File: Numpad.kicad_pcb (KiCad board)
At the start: 2 copper layers, 83.2 x 98.2 mm, 106 parts, among them J1 USB_C_Receptacle_USB2.0, J3 AVR-ISP-6, Q2 DMN2041L, SW10 SW_Push, SW11 SW_Push, SW12 SW_Push, SW13 SW_Push, SW14 SW_Push, SW15 SW_Push, SW16 SW_Push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

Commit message: redid the numpad quite a bit, including improving the usb and layout
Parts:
- H5: renamed from Kailh PG1350; value Choc -> Kailh PG1350 Stabilizer 2U Vert; footprint Keebio-Parts:Kailh-PG1350-2u-Custom -> Keebio-Parts:Kailh-Stabilizer-2u-Vert
- J1: footprint Connector_USB:USB_C_Receptacle_HRO_TYPE-C-31-M-12 -> Type-C:HRO-TYPE-C-31-M-13
- SW_RESET1: footprint Button_Switch_SMD:SW_SPST_SKQG_WithStem -> Keebio-Parts:SW_SPST_TL3342
- moved D125 111.7 mm to (150.2, 18.6)
- moved Q2 102.3 mm to (149.7, 11.8)
- moved R3 102.3 mm to (155.7, 16.6)
- moved C4 82.6 mm to (133.1, -4.43)
- moved C1 80.9 mm to (135.4, -10.2)
- moved C6 80.9 mm to (143.2, 18.7)
- moved C7 80.9 mm to (149.5, -1.01)
- moved R6 80.9 mm to (145.7, -9.77)
- moved C3 78.5 mm to (131.1, 15.3)
- moved C5 78.5 mm to (127.1, 19.3)
- moved Y1 78.5 mm to (129.1, 17.3)
- moved C2 78.5 mm to (127.3, 15.4)
- moved R23 74.0 mm to (135.6, 0.89)
- moved R34 72.8 mm to (140.4, 14.3)
- moved R1 72.2 mm to (130.8, 5.40)
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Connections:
- D1 pad 2: D- -> D+
- D1 pad 3: D+ -> D-
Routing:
- net RGB: track 121.9 -> 0.00 mm, vias 2 -> 0
- net RST: track 77.6 -> 0.00 mm, vias 1 -> 0
- net ROW_4: track 110.1 -> 54.0 mm, vias 2 -> 0
- net MISO: track 48.6 -> 0.00 mm, vias 1 -> 0
- net SCLK: track 41.8 -> 0.00 mm, vias 1 -> 0
- net ROW_3: track 95.4 -> 54.0 mm, vias 2 -> 0
- net MOSI: track 40.1 -> 0.00 mm, vias 1 -> 0
- net ROW_2: track 89.1 -> 54.0 mm
- net ROW_0: track 68.5 -> 47.0 mm
- net VCC: track 0.00 -> 21.3 mm, vias 0 -> 3
- net ROW_1: track 57.8 -> 36.5 mm
- net D33: track 87.6 -> 73.6 mm
- net D25: track 87.6 -> 73.7 mm
- net D29: track 87.5 -> 73.6 mm
- net D37: track 69.4 -> 55.6 mm
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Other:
- board size 83.2 x 98.2 mm -> 75 x 104 mm

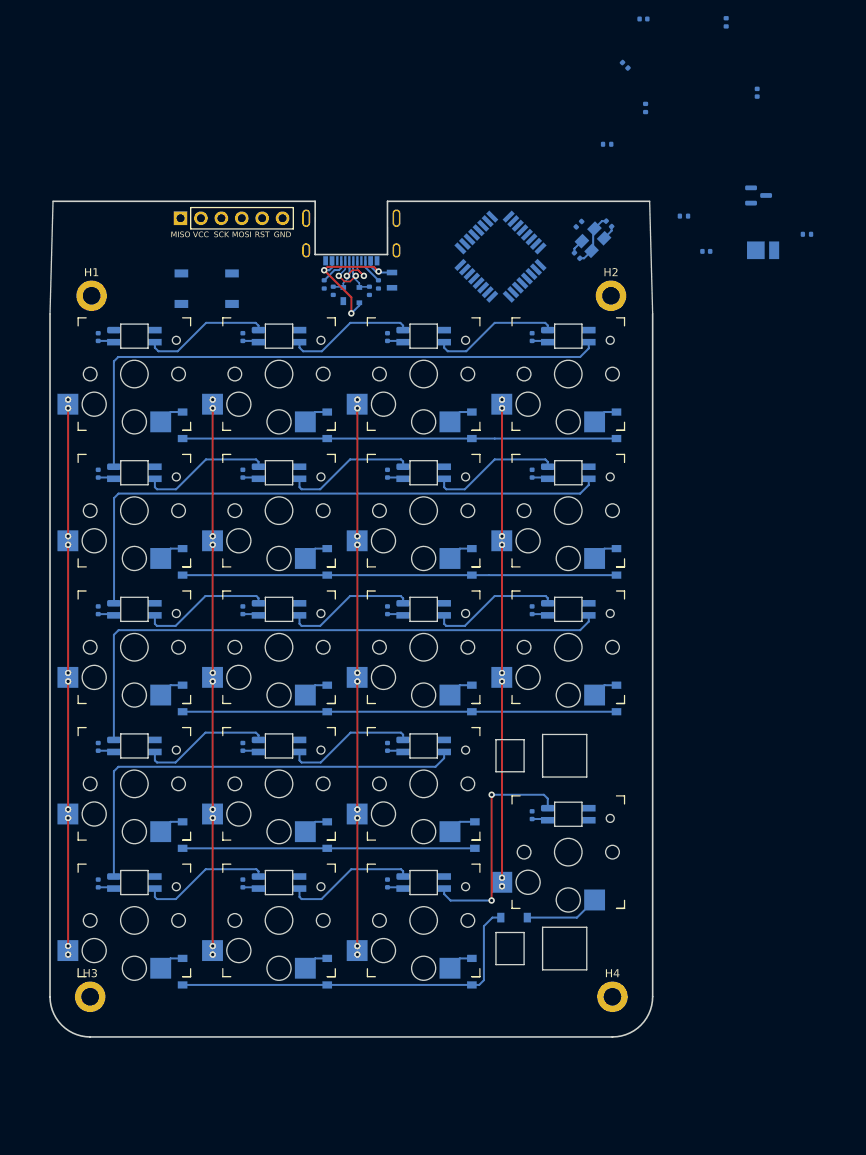
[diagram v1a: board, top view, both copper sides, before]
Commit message: did a lot of work on the numpad, basically it's "finished"
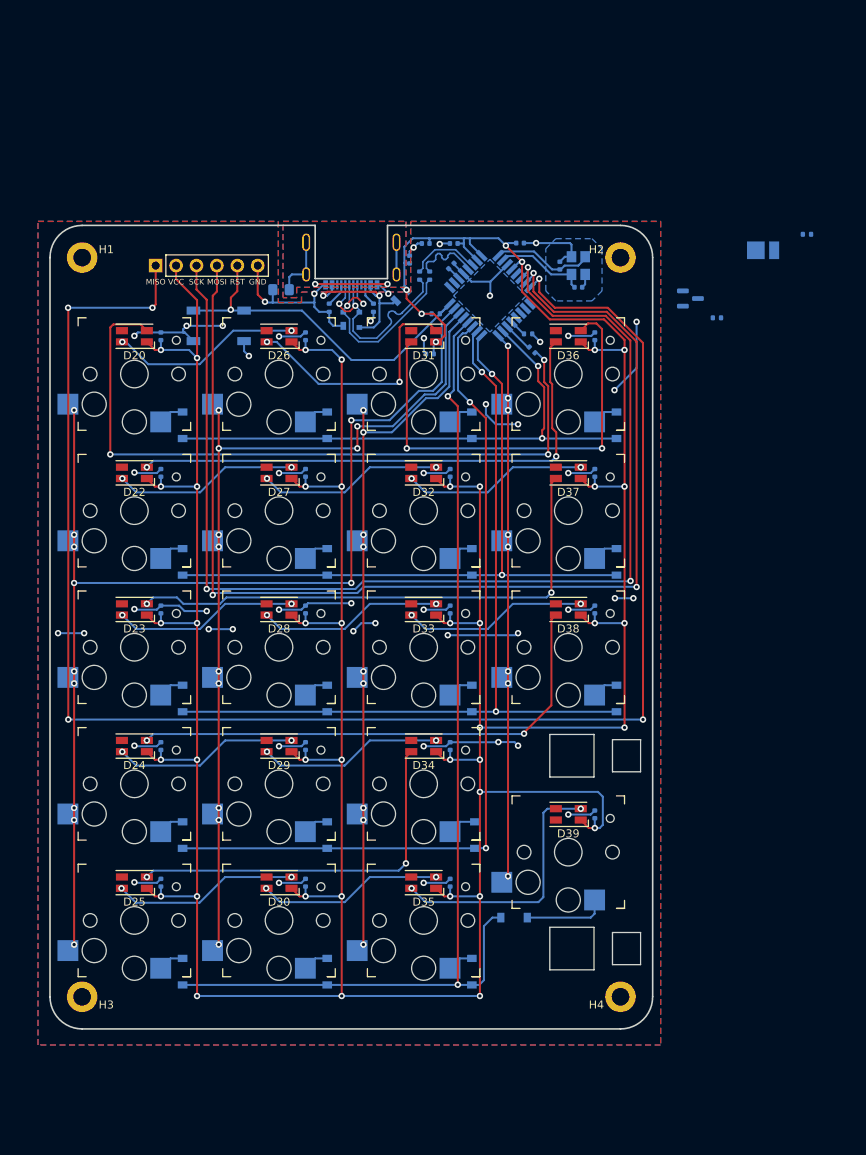
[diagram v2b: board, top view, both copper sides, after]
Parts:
- added FB1: FerriteBead_Small, Inductor_SMD:L_0805_2012Metric_Pad1.15x1.40mm_HandSolder, B.Cu at (90.2, 23.5)
- D20, D22, D23, D24, D25, D26, D27, D28, D29, D30, D31, D32, D33, D34, D35, D36, D37, D38, D39: value SK6812MINI -> NeoPixel_THT; footprint Keebio-Parts:SK6812-MINI-E -> kicad-keyboard-parts.pretty:LED_RGB_Wuerth-PLCC4_3.2x2.8mm_150141M173100; moved to F.Cu
- moved D24 74.3 mm to (72.0, 80.3)
- moved D37 74.3 mm to (126.0, 46.3)
- moved D36 59.5 mm to (126.0, 29.3)
- moved D25 51.0 mm to (72.0, 97.3)
- moved D23 49.5 mm to (72.0, 63.3)
- moved D38 49.5 mm to (126.0, 63.3)
- moved C7 45.3 mm to (108.2, 17.8), turned to 180 degrees
- moved C1 41.8 mm to (106.2, 19.8), turned to 90 degrees
- moved D28 39.8 mm to (90.0, 63.3)
- moved D33 39.8 mm to (108.0, 63.3)
- moved R6 36.8 mm to (144.5, 27.0), turned to 180 degrees
- moved R23 36.6 mm to (109.5, 26.5), turned to 0 degrees
- moved D30 34.0 mm to (90.0, 97.3)
- moved D31 34.0 mm to (108.0, 29.3)
- moved C4 33.0 mm to (111.5, 20.6), turned to 45 degrees
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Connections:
- net Net-(R2-Pad2) renamed D_P
- net Net-(R44-Pad2) renamed D_N
- D20 pad 3: RGB -> +5V
- D20 pad 4: +5V -> RGB
- D22 pad 3: Net-(D20-Pad1) -> +5V
- D22 pad 4: +5V -> D25
- D23 pad 3: Net-(D22-Pad1) -> +5V
- D23 pad 4: +5V -> D29
- D24 pad 1: D25 -> Net-(D24-Pad1)
- D24 pad 3: Net-(D23-Pad1) -> +5V
- D24 pad 4: +5V -> D33
- D25 pad 3: D25 -> +5V
- D25 pad 4: +5V -> D37
- D26 pad 3: Net-(D25-Pad1) -> +5V
- D26 pad 4: +5V -> Net-(D20-Pad1)
- D27 pad 3: Net-(D26-Pad1) -> +5V
- D27 pad 4: +5V -> Net-(D22-Pad1)
- D28 pad 1: D29 -> Net-(D28-Pad1)
- D28 pad 3: Net-(D27-Pad1) -> +5V
- D28 pad 4: +5V -> Net-(D23-Pad1)
- D29 pad 3: D29 -> +5V
- D29 pad 4: +5V -> Net-(D24-Pad1)
- D30 pad 3: Net-(D29-Pad1) -> +5V
- D30 pad 4: +5V -> Net-(D25-Pad1)
- D31 pad 3: Net-(D30-Pad1) -> +5V
- D31 pad 4: +5V -> Net-(D26-Pad1)
- D32 pad 1: D33 -> Net-(D32-Pad1)
- D32 pad 3: Net-(D31-Pad1) -> +5V
- D32 pad 4: +5V -> Net-(D27-Pad1)
- D33 pad 3: D33 -> +5V
- D33 pad 4: +5V -> Net-(D28-Pad1)
- D34 pad 1: Net-(D34-Pad1) -> D37
- D34 pad 3: Net-(D33-Pad1) -> +5V
- D34 pad 4: +5V -> Net-(D29-Pad1)
- D35 pad 1: D37 -> Net-(D35-Pad1)
- D35 pad 3: Net-(D34-Pad1) -> +5V
- D35 pad 4: +5V -> Net-(D30-Pad1)
- D36 pad 1: unconnected-(D36-Pad1) -> D25
- D36 pad 3: Net-(D36-Pad3) -> +5V
- D36 pad 4: +5V -> Net-(D31-Pad1)
- D37 pad 1: Net-(D37-Pad1) -> D29
- D37 pad 3: D37 -> +5V
- D37 pad 4: +5V -> Net-(D32-Pad1)
- D38 pad 1: Net-(D38-Pad1) -> D33
- D38 pad 3: Net-(D37-Pad1) -> +5V
- D38 pad 4: +5V -> Net-(D33-Pad1)
- D39 pad 1: Net-(D36-Pad3) -> unconnected-(D39-Pad1)
- D39 pad 3: Net-(D38-Pad1) -> +5V
- D39 pad 4: +5V -> Net-(D35-Pad1)
- J1 pad S1: GND -> Earth
- R34 pad 1: Net-(R34-Pad1) -> GND
- R34 pad 2: GND -> Net-(R34-Pad2)
- U1 pad 11: ROW_1 -> unconnected-(U1-Pad11)
- U1 pad 12: ROW_2 -> NUM_LOCK_PWM
- U1 pad 13: Net-(R34-Pad1) -> Net-(R34-Pad2)
- U1 pad 14: ROW_3 -> Net-(R1-Pad1)
- U1 pad 16: unconnected-(U1-Pad16) -> COL_3
- U1 pad 17: COL_0 -> ROW_3
- U1 pad 18: COL_1 -> ROW_2
- U1 pad 19: COL_2 -> ROW_1
- U1 pad 20: COL_3 -> ROW_0
- U1 pad 21: NUM_LOCK_PWM -> COL_2
- U1 pad 22: unconnected-(U1-Pad22) -> COL_1
- U1 pad 23: Net-(R1-Pad1) -> COL_0
- U1 pad 9: ROW_0 -> unconnected-(U1-Pad9)
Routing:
- net +5V: track 38.5 -> 553.1 mm, vias 0 -> 46
- net MISO: track 0.00 -> 204.3 mm, vias 0 -> 5
- net GND: track 7.20 -> 185.1 mm, vias 0 -> 49
- net MOSI: track 0.00 -> 144.3 mm, vias 0 -> 3
- net SCLK: track 0.00 -> 143.9 mm, vias 0 -> 3
- net RGB: track 0.00 -> 88.8 mm, vias 0 -> 3
- net ROW_0: track 47.0 -> 131.0 mm, vias 0 -> 2
- net COL_0: track 63.8 -> 144.3 mm, vias 10 -> 11
- net ROW_1: track 36.5 -> 105.1 mm, vias 0 -> 2
- net ROW_2: track 54.0 -> 102.7 mm, vias 0 -> 2
- net COL_1: track 63.8 -> 109.2 mm, vias 10 -> 11
- net RST: track 0.00 -> 44.9 mm, vias 0 -> 1
- net Net-(D31-Pad1): track 16.4 -> 55.9 mm, vias 0 -> 2
- net Net-(D35-Pad1): track 0.00 -> 32.7 mm, vias 0 -> 2
- net ROW_3: track 54.0 -> 84.5 mm, vias 0 -> 2
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- added copper zone on B.Cu, net Earth
- added copper zone on F.Cu, net Earth
- added copper zone on B.Cu, net GND
- added copper zone on F.Cu, net GND
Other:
- board size 75 x 104 mm -> 75 x 100 mm

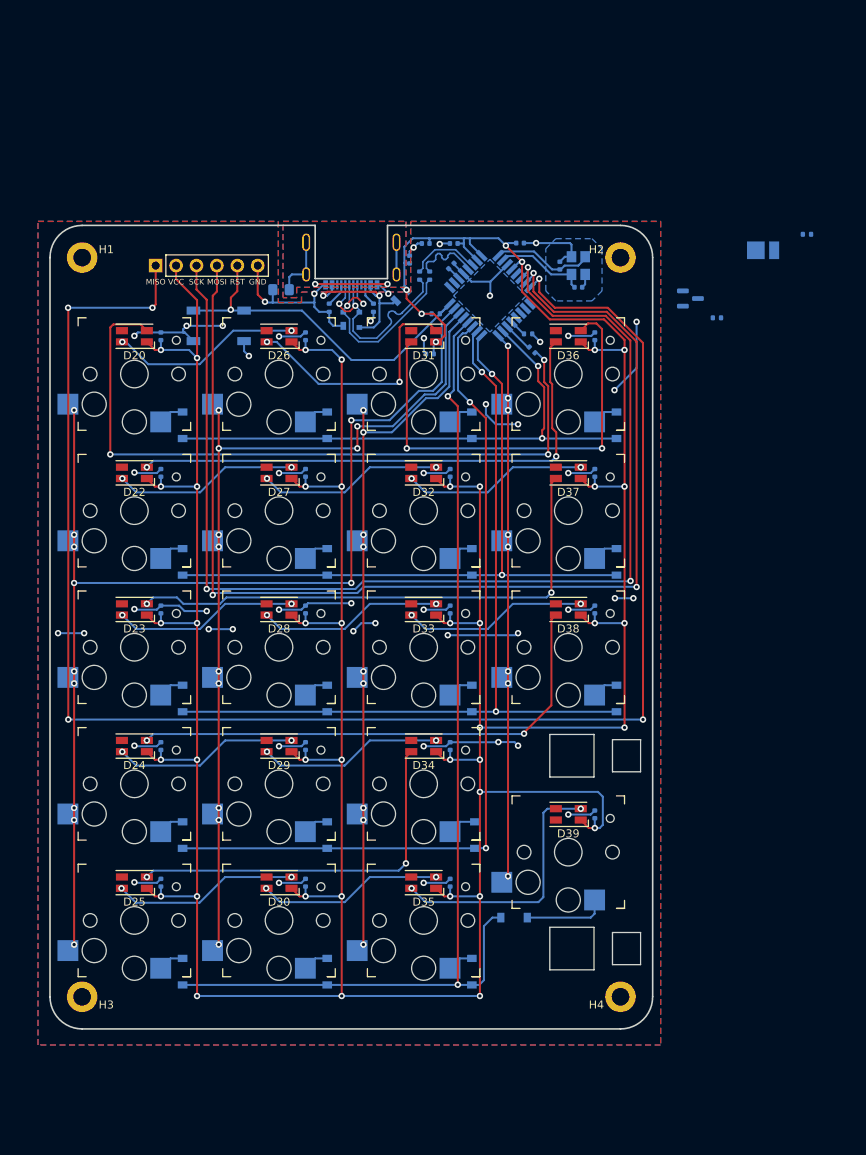
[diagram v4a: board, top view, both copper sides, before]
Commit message: Updated numpad's power traces to be thicker
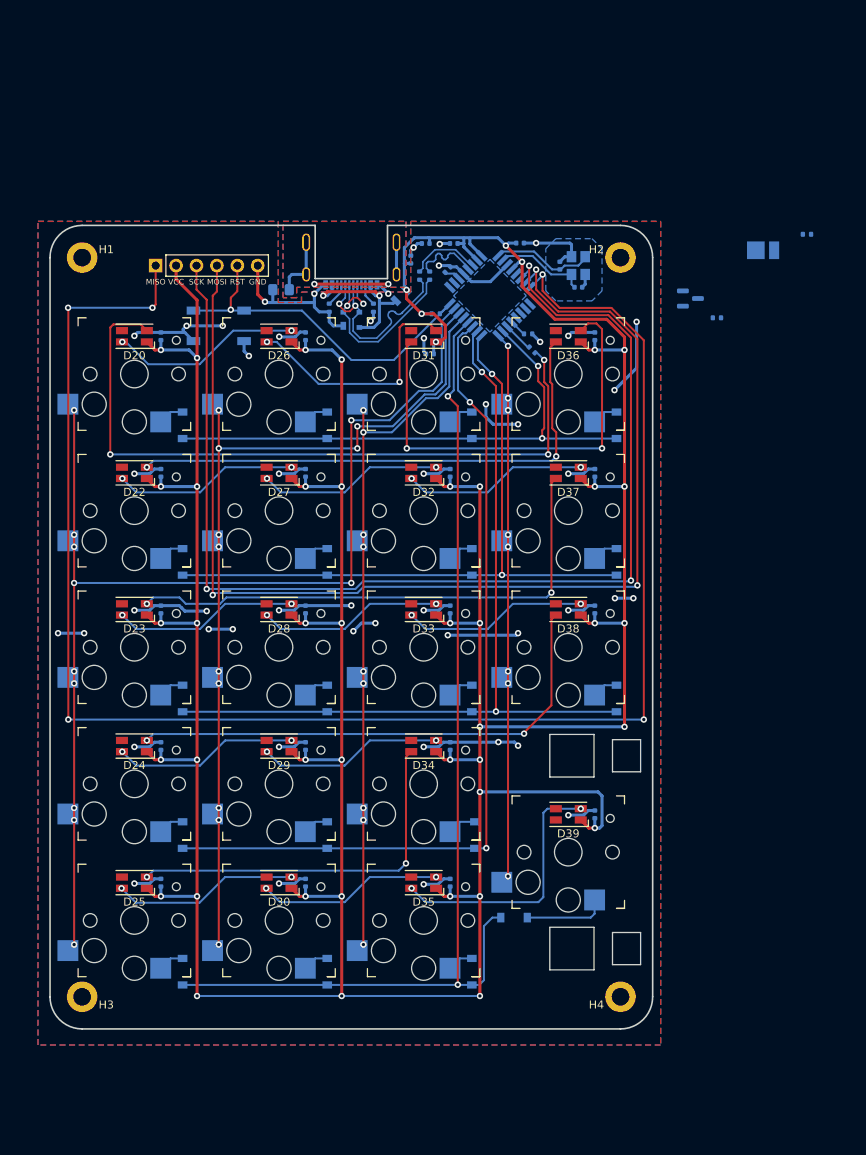
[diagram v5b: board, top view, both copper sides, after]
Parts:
- moved C4 0.64 mm to (111.0, 21.0)
- moved C1 0.15 mm to (106.4, 19.8)
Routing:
- net MISO: track 204.3 -> 205.4 mm
- net MOSI: track 144.3 -> 145.1 mm
- net +5V: track 553.1 -> 553.8 mm
- net GND: track 185.1 -> 185.7 mm

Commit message: made some footprint changes
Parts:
- removed H5: Kailh PG1350 Stabilizer 2U Vert, Keebio-Parts:Kailh-Stabilizer-2u-Vert
- SW21: footprint keyswitches.pretty-2:Kailh_socket_PG1350 -> keyswitches.pretty-2:Kailh_socket_PG1350_2U_Vert

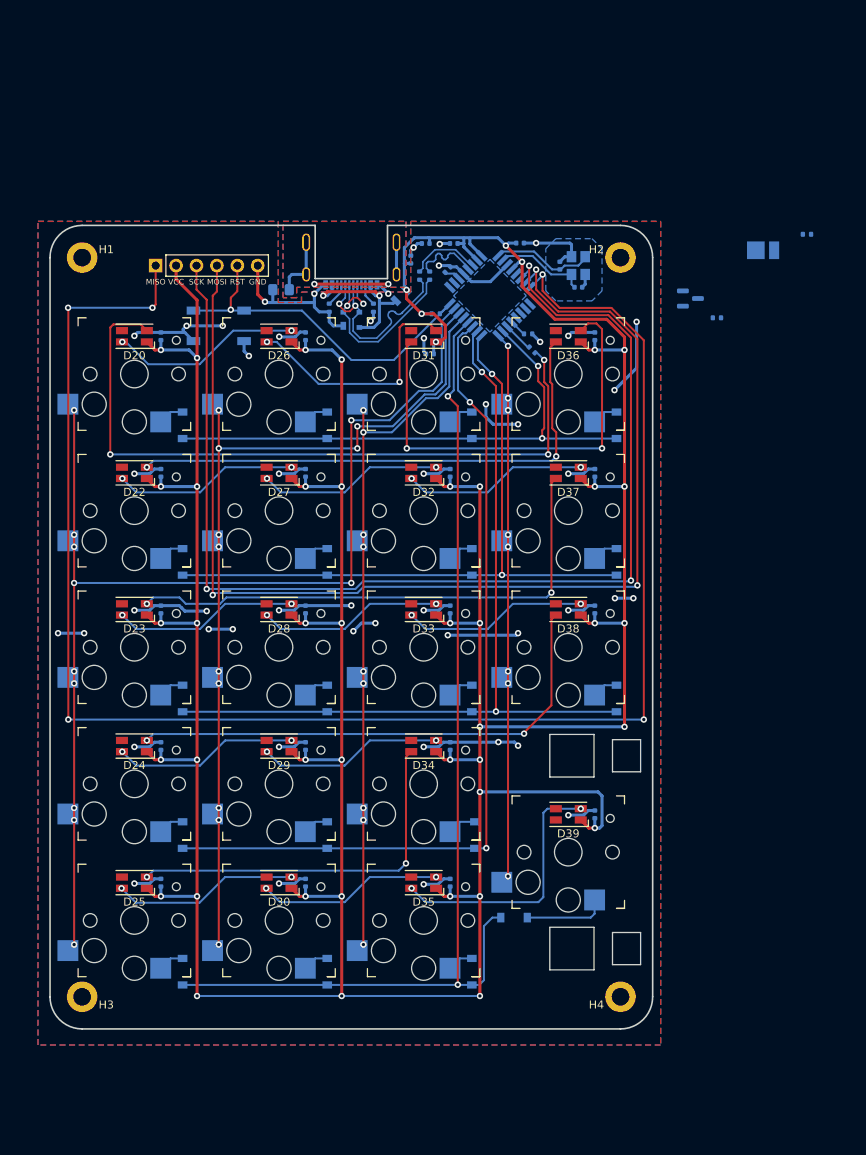
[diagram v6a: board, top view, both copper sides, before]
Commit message: did some via adjustments and decided to not go ahead with num lock light
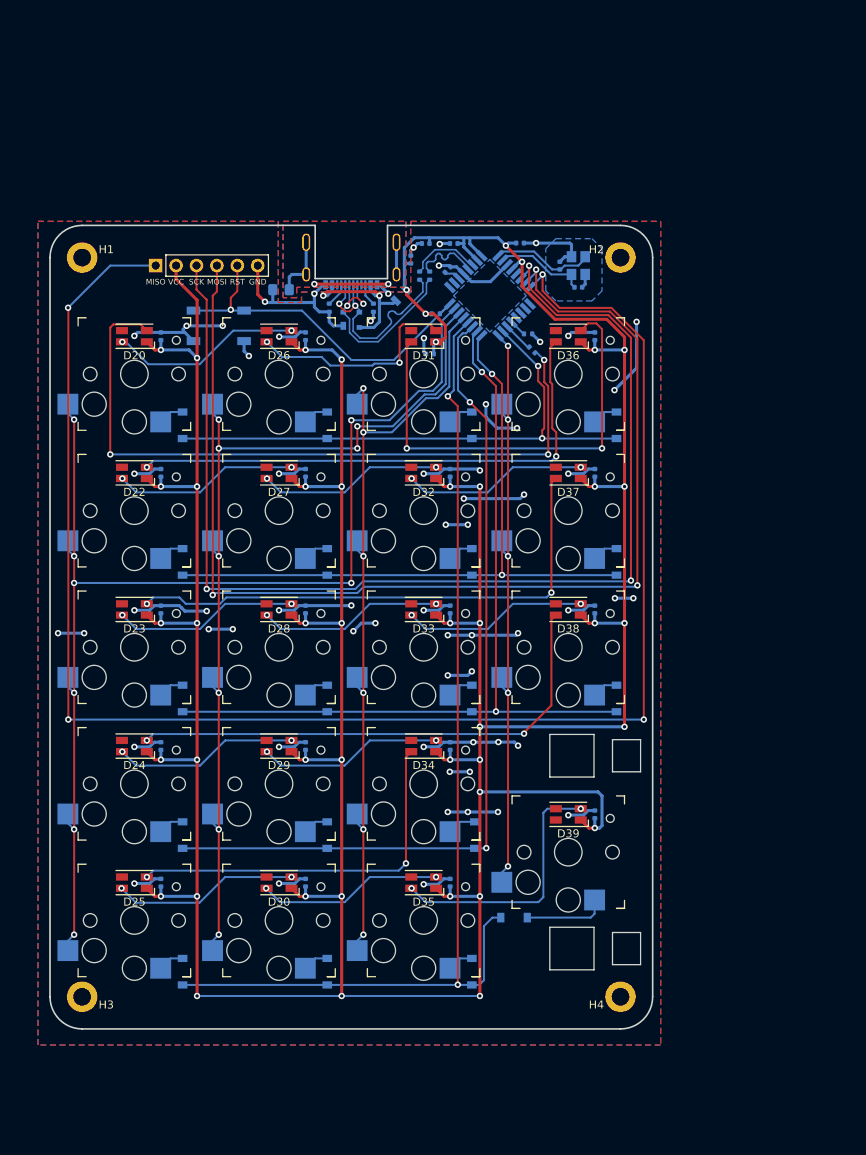
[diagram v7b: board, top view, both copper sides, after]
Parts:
- removed D125: LED, LED_SMD:LED_PLCC_2835
- removed Q2: DMN2041L, Package_TO_SOT_SMD:SOT-23
- removed R3: 470, Resistor_SMD:R_0402_1005Metric
- removed R6: 1k, Resistor_SMD:R_0402_1005Metric
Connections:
- net COL_0 renamed /COL_0
- net COL_1 renamed /COL_1
- net COL_2 renamed /COL_2
- net COL_3 renamed /COL_3
- net D+ renamed /D+
- net D- renamed /D-
- net D25 renamed /D25
- net D29 renamed /D29
- net D33 renamed /D33
- net D37 renamed /D37
- net D_N renamed /D_N
- net D_P renamed /D_P
- net MISO renamed /MISO
- net MOSI renamed /MOSI
- net RGB renamed /RGB
- net ROW_0 renamed /ROW_0
- net ROW_1 renamed /ROW_1
- net ROW_2 renamed /ROW_2
- net ROW_3 renamed /ROW_3
- net ROW_4 renamed /ROW_4
- net RST renamed /RST
- net SCLK renamed /SCLK
- U1 pad 12: NUM_LOCK_PWM -> /NUM_LOCK_PWM
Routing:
- net GND: track 185.7 -> 212.0 mm, vias 49 -> 63
- net /COL_2: track 88.9 -> 101.7 mm, vias 9 -> 6
- net /COL_1: track 109.2 -> 118.1 mm, vias 11 -> 8
- net /COL_0: track 144.3 -> 153.1 mm, vias 11 -> 8
- net /COL_3: track 67.7 -> 75.5 mm, vias 8 -> 5
- net Net-(D26-Pad1): track 30.6 -> 27.3 mm
- net /MISO: track 205.4 -> 202.6 mm, vias 5 -> 4
- net +5V: track 553.8 -> 553.1 mm
